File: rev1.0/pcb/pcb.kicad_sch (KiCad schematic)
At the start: 15 parts, among them J1 AVR-ISP-6, SW1 SW_Push, U1 ATMEGA32U4, Y1 16MHz

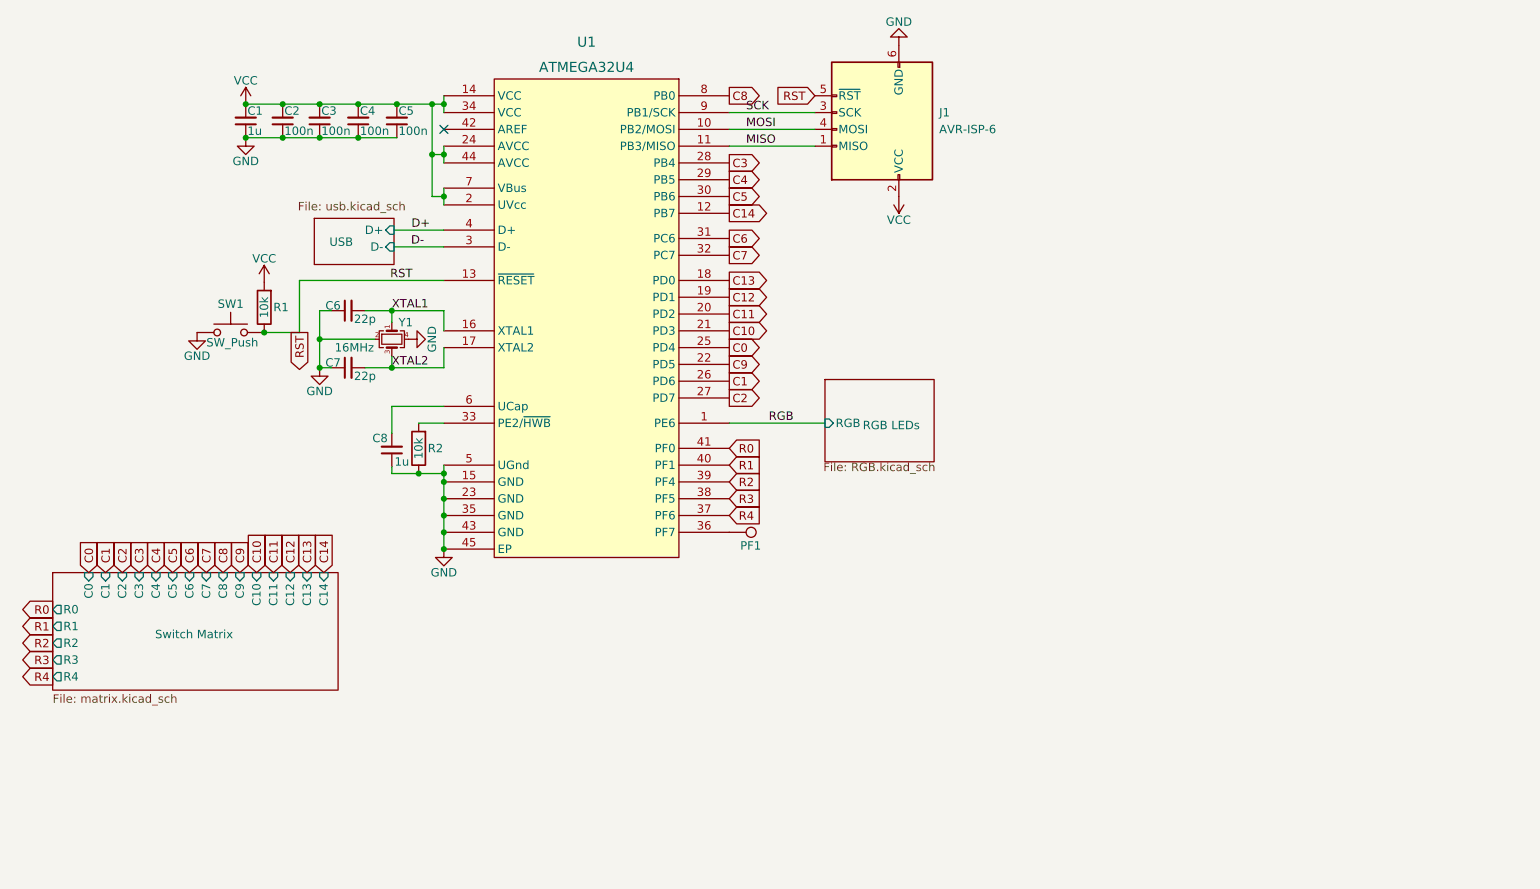
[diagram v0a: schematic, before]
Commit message: rp2040 port: updated schematic and fixed footprints
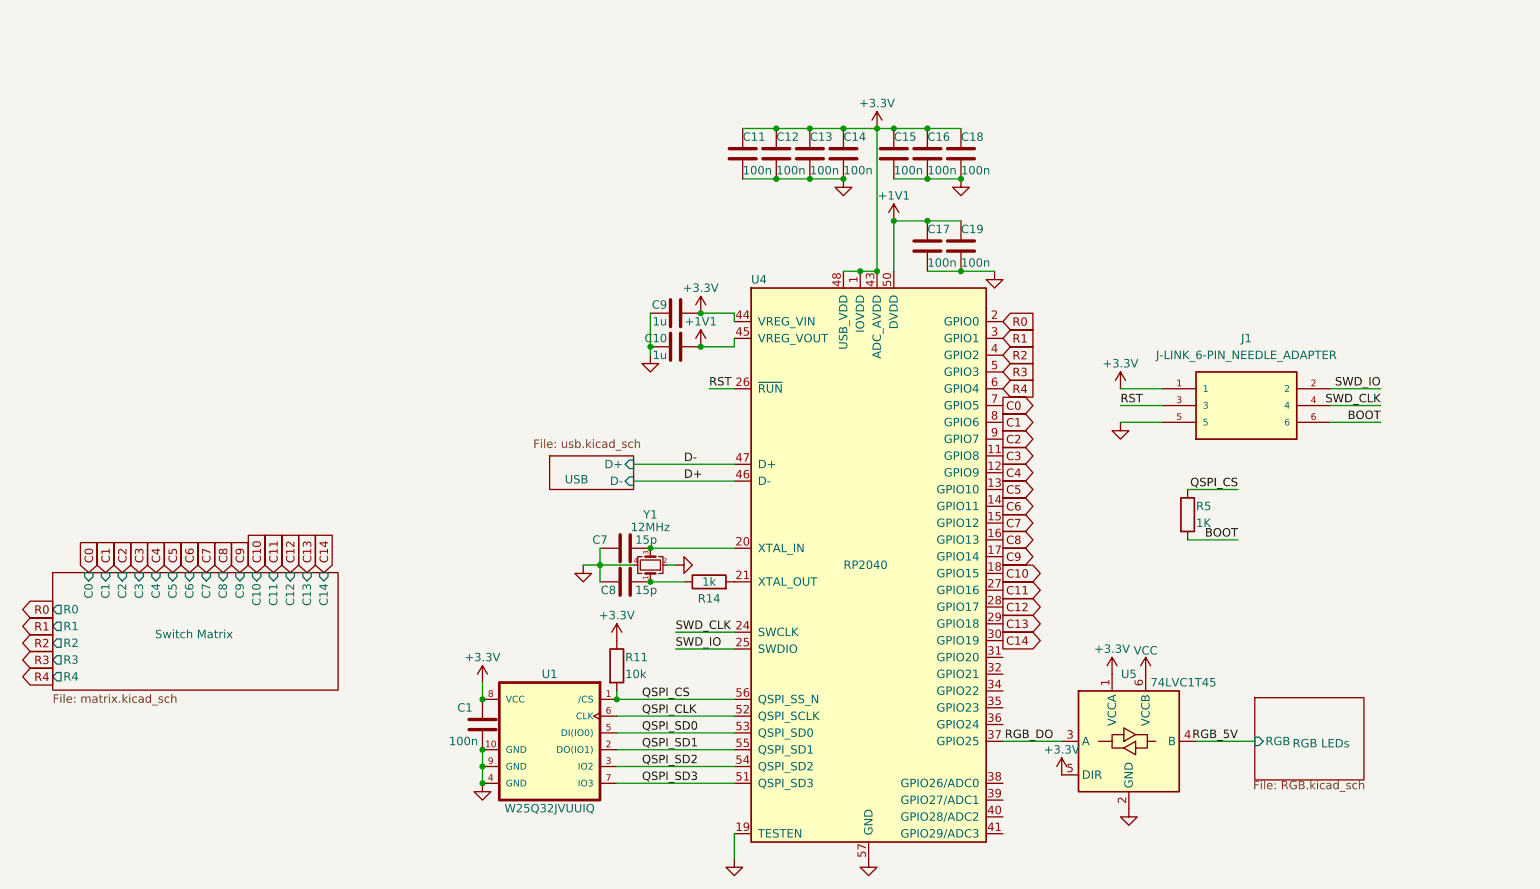
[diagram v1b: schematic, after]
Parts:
- removed C1, C8: 1u, Capacitor_SMD:C_0603_1608Metric, symbol Device:C_Small
- removed C2, C3, C4, C5: 100n, Capacitor_SMD:C_0603_1608Metric, symbol Device:C_Small
- removed C6, C7: 22p, Capacitor_SMD:C_0603_1608Metric, symbol Device:C_Small
- removed J1: AVR-ISP-6, 0xcb:AVR_PROG_2.54_THT, symbol Connector:AVR-ISP-6
- removed PF1: TestPoint, TestPoint:TestPoint_Pad_D1.5mm, symbol Connector:TestPoint
- removed R1, R2: 10k, Resistor_SMD:R_0603_1608Metric, symbol Device:R
- removed SW1: SW_Push, Button_Switch_SMD:SW_SPST_TL3342, symbol Switch:SW_Push
- removed U1: ATMEGA32U4, 0xcb:QFN-44-1EP_7x7mm_P0.5mm_EP5.2x5.2mm_ThermalVias, symbol 0xcb:ATMEGA32U4
- added C1, C11, C12, C13, C14, C15, C16, C17, C18, C19: 100n, Capacitor_SMD:C_0201_0603Metric, symbol Device:C
- added C10, C9: 1u, Capacitor_SMD:C_0201_0603Metric, symbol Device:C
- added C7, C8: 15p, Capacitor_SMD:C_0201_0603Metric, symbol Device:C
- added J1: J-LINK_6-PIN_NEEDLE_ADAPTER, 0xcb:J-LINK_6-PIN_NEEDLE_ADAPTER_SMALL, symbol 0xcb:J-LINK_6-PIN_NEEDLE_ADAPTER
- added R11: 10k, Resistor_SMD:R_0201_0603Metric, symbol Device:R
- added R14: 1k, Resistor_SMD:R_0201_0603Metric, symbol Device:R
- added R5: 1K, Resistor_SMD:R_0201_0603Metric, symbol Device:R
- added U1: W25Q32JVUUIQ, 0xcb:W25Q32JVUUIQ, symbol 0xcb:W25Q32JVUUIQ
- added U4: RP2040, Package_DFN_QFN:QFN-56-1EP_7x7mm_P0.4mm_EP3.2x3.2mm, symbol 0xcb:RP2040
- added U5: 74LVC1T45, Package_TO_SOT_SMD:SOT-563, symbol Logic_LevelTranslator:SN74LVC1T45DRL
- Y1: value 16MHz -> 12MHz; footprint 0xcb:Crystal_SMD_3225-4Pin_3.2x2.5mm -> Crystal:Crystal_SMD_2520-4Pin_2.5x2.0mm; JLC Basic (none) -> N; LCSC (none) -> C2149204; MPN  (none) -> 2TJ412000HYGBC; Manufacturer (none) -> JYJE; Substitute (none) -> N
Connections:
- net C0: now also U4.7 (GPIO5)
- net C1: now also U4.8 (GPIO6)
- net C10: now also U4.18 (GPIO15)
- net C11: now also U4.27 (GPIO16)
- net C12: now also U4.28 (GPIO17)
- net C13: now also U4.29 (GPIO18)
- net C14: now also U4.30 (GPIO19)
- net C2: now also U4.9 (GPIO7)
- net C3: now also U4.11 (GPIO8)
- net C4: now also U4.12 (GPIO9)
- net C5: now also U4.13 (GPIO10)
- net C6: now also U4.14 (GPIO11)
- net C7: now also U4.15 (GPIO12)
- net C8: now also U4.16 (GPIO13)
- net C9: now also U4.17 (GPIO14)
- net D+: now also U4.46 (D-)
- net D-: now also U4.47 (D+)
- net GND: now also C1.2, C10.1, C11.2, C12.2, C13.2, C14.2, C15.2, C16.2, C17.2, C18.2, C19.2, C7.1, C8.1, C9.1, J1.5, U1.10 (GND), U1.4 (GND), U1.9 (GND), U4.19 (TESTEN), U4.57 (GND), U5.2 (GND)
- net R0: now also U4.2 (GPIO0)
- net R1: now also U4.3 (GPIO1)
- net R2: now also U4.4 (GPIO2)
- net R3: now also U4.5 (GPIO3)
- net R4: now also U4.6 (GPIO4)
- net RST: now also J1.3, U4.26 (~{RUN})
- net VCC: now also U5.6 (VCCB)
- net XTAL1: no longer names the net of Y1.1
- net XTAL1: now also C8.2, R14.1
- net XTAL2: no longer names the net of Y1.3
- net XTAL2: now also C7.2, U4.20 (XTAL_IN)
- new net: R14.2, U4.21 (XTAL_OUT)
- new net +1V1: C10.2, C17.1, C19.1, U4.23 (DVDD), U4.45 (VREG_VOUT), U4.50 (DVDD)
- new net +3.3V: C1.1, C11.1, C12.1, C13.1, C14.1, C15.1, C16.1, C18.1, C9.2, J1.1, R11.1, U1.8 (VCC), U4.1 (IOVDD), U4.10 (IOVDD), U4.22 (IOVDD), U4.33 (IOVDD), U4.42 (IOVDD), U4.43 (ADC_AVDD), U4.44 (VREG_VIN), U4.48 (USB_VDD), U4.49 (IOVDD), U5.1 (VCCA), U5.5 (DIR)
- new net BOOT: J1.6, R5.2
- new net QSPI_CLK: U1.6 (CLK), U4.52 (QSPI_SCLK)
- new net QSPI_CS: R11.2, R5.1, U1.1 (/CS), U4.56 (QSPI_SS_N)
- new net QSPI_SD0: U1.5 (DI(IO0)), U4.53 (QSPI_SD0)
- new net QSPI_SD1: U1.2 (DO(IO1)), U4.55 (QSPI_SD1)
- new net QSPI_SD2: U1.3 (IO2), U4.54 (QSPI_SD2)
- new net QSPI_SD3: U1.7 (IO3), U4.51 (QSPI_SD3)
- new net RGB_5V: U5.4 (B)
- new net RGB_DO: U4.37 (GPIO25), U5.3 (A)
- new net SWD_CLK: J1.4, U4.24 (SWCLK)
- new net SWD_IO: J1.2, U4.25 (SWDIO)
- no-connect marks 1 -> 0

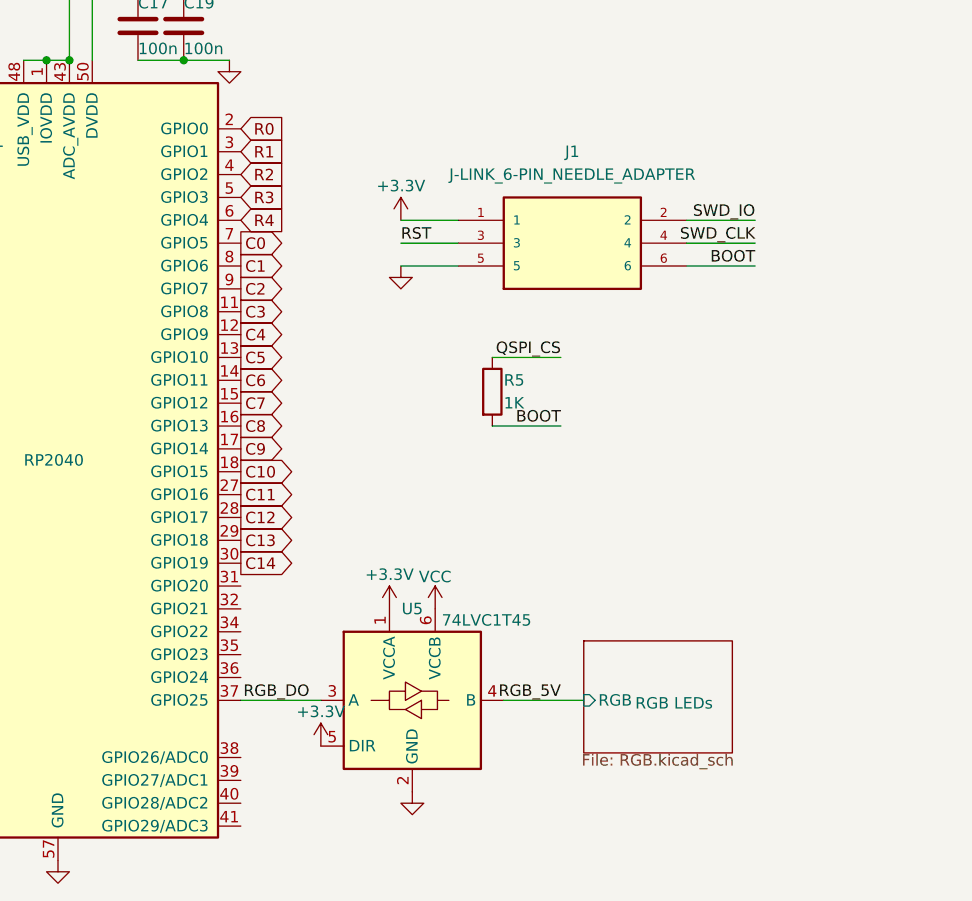
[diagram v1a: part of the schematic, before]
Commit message: routing of RP2040
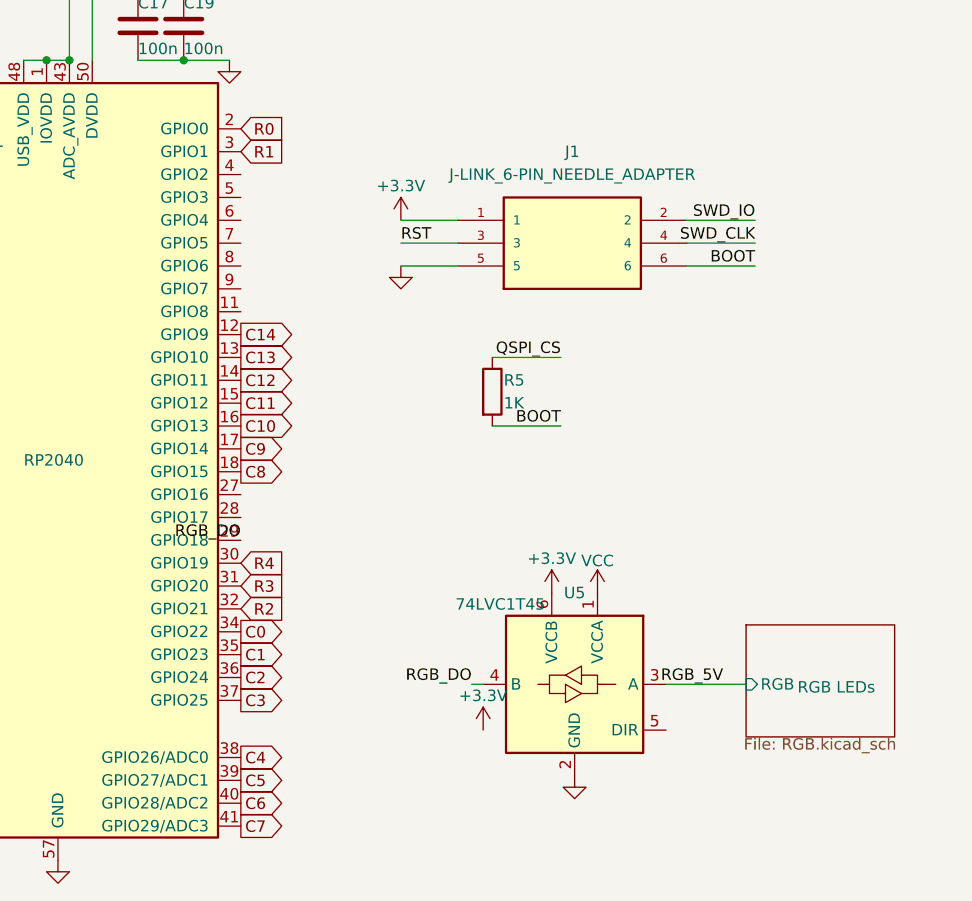
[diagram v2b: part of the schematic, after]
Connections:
- net +3.3V: now also U5.6 (VCCB); no longer U5.1 (VCCA), U5.5 (DIR)
- net C0: now also U4.34 (GPIO22); no longer U4.7 (GPIO5)
- net C1: now also U4.35 (GPIO23); no longer U4.8 (GPIO6)
- net C10: now also U4.16 (GPIO13); no longer U4.18 (GPIO15)
- net C11: now also U4.15 (GPIO12); no longer U4.27 (GPIO16)
- net C12: now also U4.14 (GPIO11); no longer U4.28 (GPIO17)
- net C13: now also U4.13 (GPIO10); no longer U4.29 (GPIO18)
- net C14: now also U4.12 (GPIO9); no longer U4.30 (GPIO19)
- net C2: now also U4.36 (GPIO24); no longer U4.9 (GPIO7)
- net C3: now also U4.37 (GPIO25); no longer U4.11 (GPIO8)
- net C4: now also U4.38 (GPIO26/ADC0); no longer U4.12 (GPIO9)
- net C5: now also U4.39 (GPIO27/ADC1); no longer U4.13 (GPIO10)
- net C6: now also U4.40 (GPIO28/ADC2); no longer U4.14 (GPIO11)
- net C7: now also U4.41 (GPIO29/ADC3); no longer U4.15 (GPIO12)
- net C8: now also U4.18 (GPIO15); no longer U4.16 (GPIO13)
- net R2: now also U4.32 (GPIO21); no longer U4.4 (GPIO2)
- net R3: now also U4.31 (GPIO20); no longer U4.5 (GPIO3)
- net R4: now also U4.30 (GPIO19); no longer U4.6 (GPIO4)
- net RGB_5V: now also U5.3 (A); no longer U5.4 (B)
- net RGB_DO: now also U4.29 (GPIO18), U5.4 (B); no longer U4.37 (GPIO25), U5.3 (A)
- net VCC: now also U5.1 (VCCA); no longer U5.6 (VCCB)
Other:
- moved on the sheet: U5

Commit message: fixup and add prod
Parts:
- C1, C11, C12, C13, C14, C15, C16, C17, C18, C19: LCSC C1525 -> C576431
- C10, C9: LCSC C52923 -> C237458
- C7, C8: JLCPCB_CORRECTION (none) -> 0; 0; 90; LCSC C1548 -> C85891
- R11: JLCPCB_CORRECTION (none) -> 0; 0; 90; LCSC C25744 -> C138117
- R14: JLCPCB_CORRECTION (none) -> 0; 0; 90; LCSC C11702 -> C138165
- U1: JLCPCB_CORRECTION (none) -> 0; 0; 180
- U4: JLCPCB_CORRECTION (none) -> 0; 0; 90
- Y1: JLCPCB_CORRECTION (none) -> 0; 0; 270
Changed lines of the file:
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@@
       (effects (font (size 1.27 1.27)) hide)
     )
-    (property "LCSC" "C1525" (at 149.86 35.56 0)
+    (property "LCSC" "C576431" (at 149.86 35.56 0)
       (effects (font (size 1.27 1.27)) hide)
     )
@@
       (effects (font (size 1.27 1.27)) hide)
     )
-    (property "LCSC" "C11702" (at 129.54 100.33 0)
+    (property "LCSC" "C138165" (at 129.54 100.33 0)
       (effects (font (size 1.27 1.27)) hide)
     )
@@
     )
     (property "Substitute" "Y" (at 129.54 100.33 0)
+      (effects (font (size 1.27 1.27)) hide)
+    )
+    (property "JLCPCB_CORRECTION" "0; 0; 90" (at 129.54 100.33 0)
       (effects (font (size 1.27 1.27)) hide)
     )
@@
       (effects (font (size 1.27 1.27)) hide)
     )
-    (property "LCSC" "C1525" (at 157.48 35.56 0)
+    (property "LCSC" "C576431" (at 157.48 35.56 0)
       (effects (font (size 1.27 1.27)) hide)
     )
@@
       (effects (font (size 1.27 1.27)) hide)
     )
-    (property "LCSC" "C1525" (at 162.56 49.53 0)
+    (property "LCSC" "C576431" (at 162.56 49.53 0)
       (effects (font (size 1.27 1.27)) hide)
     )
@@
       (effects (font (size 1.27 1.27)) hide)
     )
-    (property "LCSC" "C1525" (at 162.56 35.56 0)
+    (property "LCSC" "C576431" (at 162.56 35.56 0)
       (effects (font (size 1.27 1.27)) hide)
     )
@@
       (effects (font (size 1.27 1.27)) hide)
     )
-    (property "LCSC" "C52923" (at 124.46 59.69 0)
+    (property "LCSC" "C237458" (at 124.46 59.69 0)
       (effects (font (size 1.27 1.27)) hide)
     )
@@
     )
     (property "Substitute" "N" (at 153.67 97.79 0)
+      (effects (font (size 1.27 1.27)) hide)
+    )
+    (property "JLCPCB_CORRECTION" "0; 0; 90" (at 153.67 97.79 0)
       (effects (font (size 1.27 1.27)) hide)
     )
@@
       (effects (font (size 1.27 1.27)) (justify left bottom) hide)
     )
-    (property "LCSC" "~" (at 210.82 73.66 0)
+    (property "LCSC" "" (at 210.82 73.66 0)
       (effects (font (size 1.27 1.27)) hide)
     )
@@
       (effects (font (size 1.27 1.27)) hide)
     )
+    (property "JLCPCB_CORRECTION" "0; 0; 270" (at 120.65 97.79 0)
+      (effects (font (size 1.27 1.27)) hide)
+    )
     (pin "1")
     (pin "2")
@@
       (effects (font (size 1.27 1.27)) hide)
     )
-    (property "LCSC" "C1525" (at 167.64 49.53 0)
+    (property "LCSC" "C576431" (at 167.64 49.53 0)
       (effects (font (size 1.27 1.27)) hide)
     )
@@
       (effects (font (size 1.27 1.27)) hide)
     )
-    (property "LCSC" "C1525" (at 144.78 35.56 0)
+    (property "LCSC" "C576431" (at 144.78 35.56 0)
       (effects (font (size 1.27 1.27)) hide)
     )
@@
       (effects (font (size 1.27 1.27)) hide)
     )
-    (property "LCSC" "C1525" (at 134.62 35.56 0)
+    (property "LCSC" "C576431" (at 134.62 35.56 0)
       (effects (font (size 1.27 1.27)) hide)
     )
@@
       (effects (font (size 1.27 1.27)) hide)
     )
-    (property "LCSC" "C52923" (at 124.46 64.77 0)
+    (property "LCSC" "C237458" (at 124.46 64.77 0)
       (effects (font (size 1.27 1.27)) hide)
     )
@@
     )
     (property "MPN " "W25Q32JVUUIQ" (at 105.41 124.46 0)
+      (effects (font (size 1.27 1.27)) hide)
+    )
+    (property "JLCPCB_CORRECTION" "0; 0; 180" (at 105.41 124.46 0)
       (effects (font (size 1.27 1.27)) hide)
     )
@@
       (effects (font (size 1.27 1.27)) hide)
     )
-    (property "LCSC" "C1525" (at 167.64 35.56 0)
+    (property "LCSC" "C576431" (at 167.64 35.56 0)
       (effects (font (size 1.27 1.27)) hide)
     )
@@
       (effects (font (size 1.27 1.27)) hide)
     )
-    (property "LCSC" "C25744" (at 115.57 113.03 0)
+    (property "LCSC" "C138117" (at 115.57 113.03 0)
       (effects (font (size 1.27 1.27)) hide)
     )
@@
     )
     (property "Substitute" "Y" (at 115.57 113.03 0)
+      (effects (font (size 1.27 1.27)) hide)
+    )
+    (property "JLCPCB_CORRECTION" "0; 0; 90" (at 115.57 113.03 0)
       (effects (font (size 1.27 1.27)) hide)
     )
@@
     )
     (property "Manufacturer" "UNI-ROYAL(Uniroyal Elec)" (at 201.93 90.17 0)
+      (effects (font (size 1.27 1.27)) hide)
+    )
+    (property "JLCPCB_CORRECTION" "" (at 201.93 90.17 0)
       (effects (font (size 1.27 1.27)) hide)
     )
@@
       (effects (font (size 1.27 1.27)) hide)
     )
-    (property "LCSC" "C1548" (at 116.84 95.25 0)
+    (property "LCSC" "C85891" (at 116.84 95.25 0)
       (effects (font (size 1.27 1.27)) hide)
     )
@@
     )
     (property "Substitute" "Y" (at 116.84 95.25 0)
+      (effects (font (size 1.27 1.27)) hide)
+    )
+    (property "JLCPCB_CORRECTION" "0; 0; 90" (at 116.84 95.25 0)
       (effects (font (size 1.27 1.27)) hide)
     )
@@
       (effects (font (size 1.27 1.27)) hide)
     )
-    (property "LCSC" "C1525" (at 139.7 35.56 0)
+    (property "LCSC" "C576431" (at 139.7 35.56 0)
       (effects (font (size 1.27 1.27)) hide)
     )
@@
       (effects (font (size 1.27 1.27)) hide)
     )
-    (property "LCSC" "C1525" (at 95.25 121.92 0)
+    (property "LCSC" "C576431" (at 95.25 121.92 0)
       (effects (font (size 1.27 1.27)) hide)
     )
@@
       (effects (font (size 1.27 1.27)) hide)
     )
-    (property "LCSC" "C1548" (at 116.84 100.33 0)
+    (property "LCSC" "C85891" (at 116.84 100.33 0)
       (effects (font (size 1.27 1.27)) hide)
     )
@@
       (effects (font (size 1.27 1.27)) hide)
     )
+    (property "JLCPCB_CORRECTION" "0; 0; 90" (at 116.84 100.33 0)
+      (effects (font (size 1.27 1.27)) hide)
+    )
